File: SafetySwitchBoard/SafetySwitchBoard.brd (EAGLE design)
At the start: 47 x 73.7 mm, 10 parts

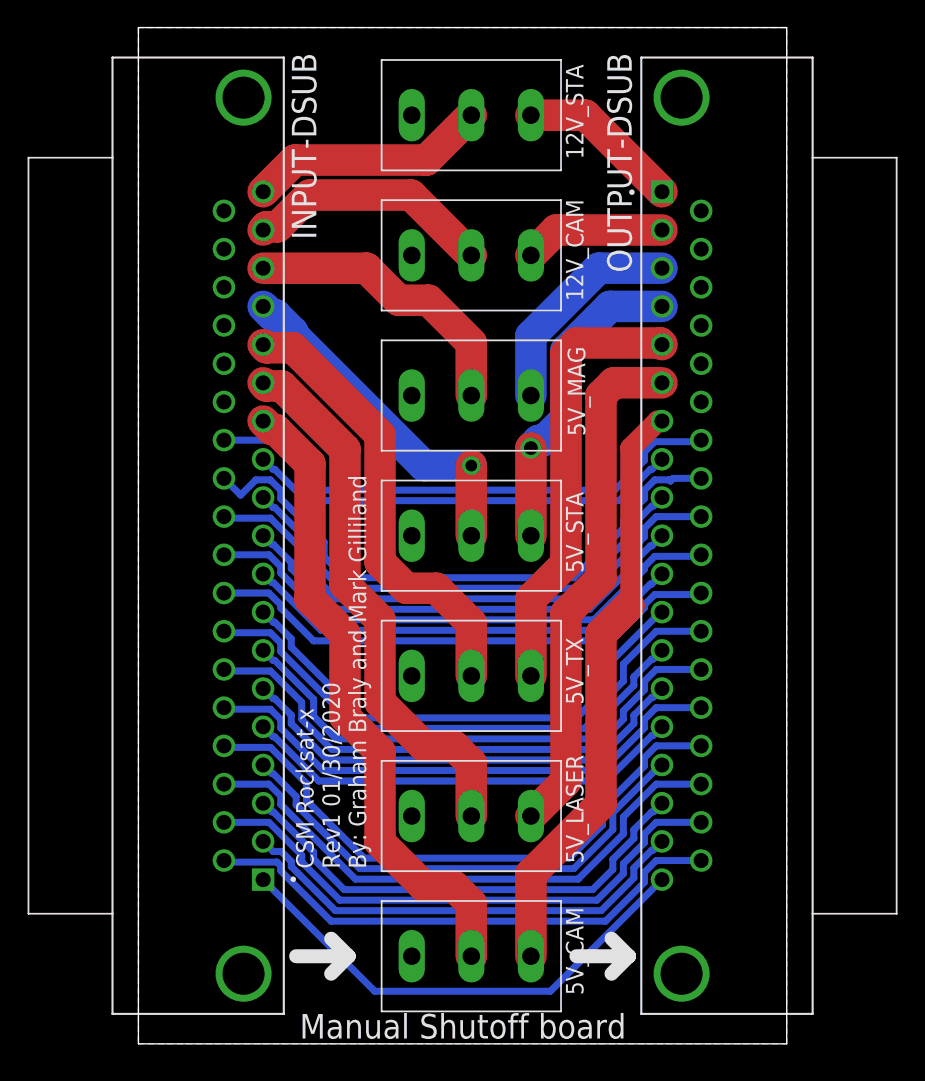
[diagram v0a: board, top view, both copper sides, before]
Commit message: Switch board diff pair rerouted
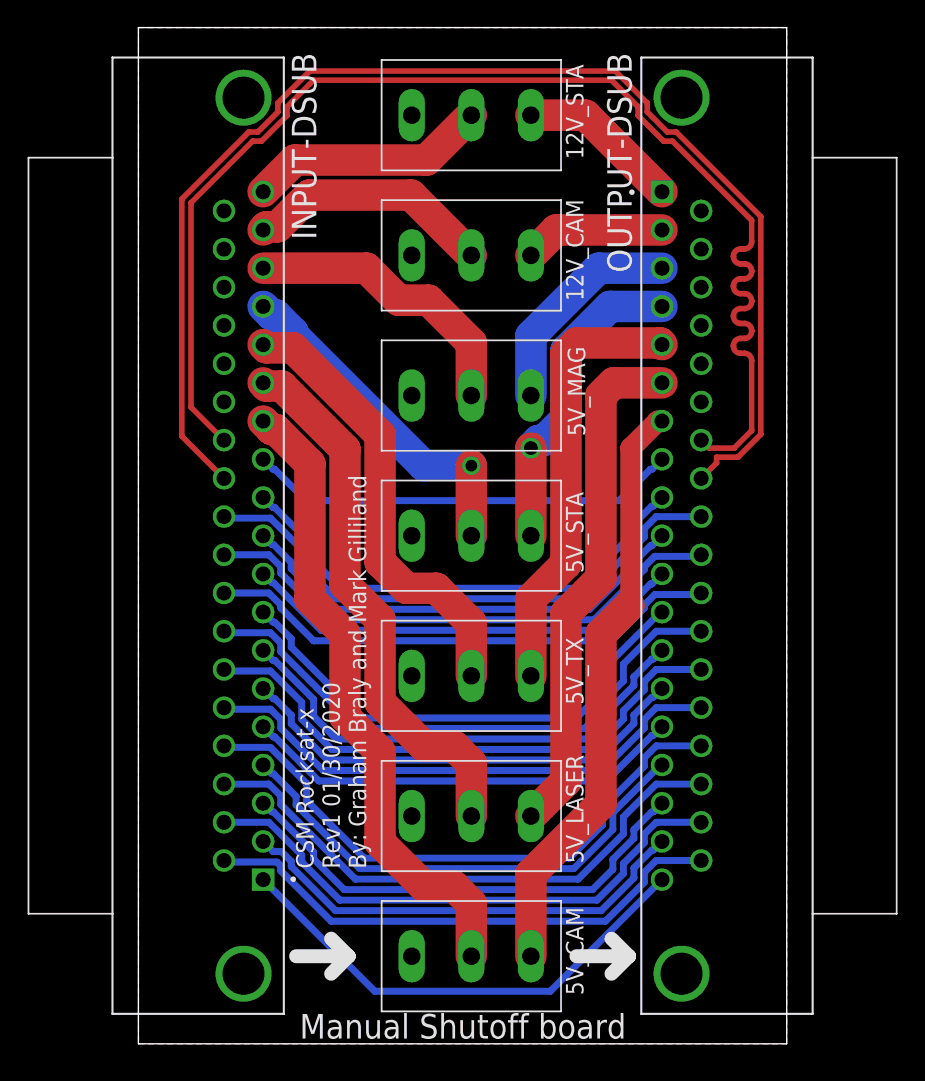
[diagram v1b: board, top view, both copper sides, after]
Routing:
- net USB-CAM_N: track 38.0 -> 92.8 mm
- net USB-CAM_P: track 43.2 -> 94.1 mm
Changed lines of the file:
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@@
 <class number="0" name="default" width="0" drill="0">
 </class>
-<class number="1" name="USB-DIFF" width="0" drill="0">
+<class number="1" name="USB-DIFF" width="0.4064" drill="0">
+<clearance class="1" value="0.254"/>
 </class>
 </classes>
@@
 <contactref element="INPUT-DSUB" pad="26"/>
 <contactref element="OUTPUT-DSUB" pad="31"/>
-<wire x1="6.2" y1="43.755" x2="9.585" y2="43.755" width="0.508" layer="16"/>
-<wire x1="34.5240375" y1="40.132" x2="36.6753" y2="42.2832625" width="0.508" layer="16"/>
-<wire x1="36.6753" y1="42.2832625" x2="36.6753" y2="42.898" width="0.508" layer="16"/>
-<wire x1="36.6753" y1="42.898" x2="37.422" y2="43.6447" width="0.508" layer="16"/>
-<wire x1="40.6797" y1="43.6447" x2="40.79" y2="43.755" width="0.508" layer="16"/>
-<wire x1="9.585" y1="43.755" x2="13.208" y2="40.132" width="0.508" layer="16"/>
-<wire x1="13.208" y1="40.132" x2="34.5240375" y2="40.132" width="0.508" layer="16"/>
-<wire x1="37.422" y1="43.6447" x2="40.6797" y2="43.6447" width="0.508" layer="16"/>
+<wire x1="6.2" y1="43.755" x2="3.81" y2="46.145" width="0.4064" layer="1"/>
+<wire x1="3.81" y1="46.145" x2="3.81" y2="60.96" width="0.4064" layer="1"/>
+<wire x1="3.81" y1="60.96" x2="8.2794" y2="65.4294" width="0.4064" layer="1"/>
+<wire x1="8.2794" y1="65.4294" x2="8.925025" y2="65.4294" width="0.4064" layer="1"/>
+<wire x1="8.925025" y1="65.4294" x2="10.7706" y2="67.274975" width="0.4064" layer="1"/>
+<wire x1="10.7706" y1="67.274975" x2="10.7706" y2="67.9206" width="0.4064" layer="1"/>
+<wire x1="10.7706" y1="67.9206" x2="12.7" y2="69.85" width="0.4064" layer="1"/>
+<wire x1="34.29" y1="69.85" x2="36.2194" y2="67.9206" width="0.4064" layer="1"/>
+<wire x1="36.2194" y1="67.9206" x2="36.2194" y2="67.274975" width="0.4064" layer="1"/>
+<wire x1="36.2194" y1="67.274975" x2="38.064975" y2="65.4294" width="0.4064" layer="1"/>
+<wire x1="38.064975" y1="65.4294" x2="38.7106" y2="65.4294" width="0.4064" layer="1"/>
+<wire x1="44.45" y1="44.45" x2="43.18" y2="43.18" width="0.4064" layer="1"/>
+<wire x1="12.7" y1="69.85" x2="34.29" y2="69.85" width="0.4064" layer="1"/>
+<wire x1="38.7106" y1="65.4294" x2="44.45" y2="59.69" width="0.4064" layer="1"/>
+<wire x1="44.45" y1="59.69" x2="44.45" y2="58.1392375" width="0.4064" layer="1"/>
+<wire x1="44.45" y1="58.1392375" x2="43.9293" y2="57.6185375" width="0.4064" layer="1" curve="-90"/>
+<wire x1="43.9293" y1="57.6185375" x2="43.652925" y2="57.6185375" width="0.4064" layer="1"/>
+<wire x1="43.652925" y1="57.6185375" x2="43.132225" y2="57.0978375" width="0.4064" layer="1" curve="90"/>
+<wire x1="43.132225" y1="57.0978375" x2="43.132225" y2="57.05811875" width="0.4064" layer="1"/>
+<wire x1="43.132225" y1="57.05811875" x2="43.652925" y2="56.53741875" width="0.4064" layer="1" curve="90"/>
+<wire x1="43.652925" y1="56.53741875" x2="43.9293" y2="56.53741875" width="0.4064" layer="1"/>
+<wire x1="43.9293" y1="56.53741875" x2="44.45" y2="56.01671875" width="0.4064" layer="1" curve="-90"/>
+<wire x1="44.45" y1="56.01671875" x2="44.45" y2="55.976996875" width="0.4064" layer="1"/>
+<wire x1="44.45" y1="55.976996875" x2="43.9293" y2="55.456296875" width="0.4064" layer="1" curve="-90"/>
+<wire x1="43.9293" y1="55.456296875" x2="43.652925" y2="55.456296875" width="0.4064" layer="1"/>
+<wire x1="43.652925" y1="55.456296875" x2="43.132225" y2="54.935596875" width="0.4064" layer="1" curve="90"/>
+<wire x1="43.132225" y1="54.935596875" x2="43.132225" y2="54.895878125" width="0.4064" layer="1"/>
+<wire x1="43.132225" y1="54.895878125" x2="43.652925" y2="54.375178125" width="0.4064" layer="1" curve="90"/>
+<wire x1="43.652925" y1="54.375178125" x2="43.9293" y2="54.375178125" width="0.4064" layer="1"/>
+<wire x1="43.9293" y1="54.375178125" x2="44.45" y2="53.854478125" width="0.4064" layer="1" curve="-90"/>
+<wire x1="44.45" y1="53.854478125" x2="44.45" y2="53.814759375" width="0.4064" layer="1"/>
+<wire x1="44.45" y1="53.814759375" x2="43.9293" y2="53.294059375" width="0.4064" layer="1" curve="-90"/>
+<wire x1="43.9293" y1="53.294059375" x2="43.652925" y2="53.294059375" width="0.4064" layer="1"/>
+<wire x1="43.652925" y1="53.294059375" x2="43.132225" y2="52.773359375" width="0.4064" layer="1" curve="90"/>
+<wire x1="43.132225" y1="52.773359375" x2="43.132225" y2="52.733640625" width="0.4064" layer="1"/>
+<wire x1="43.132225" y1="52.733640625" x2="43.652925" y2="52.212940625" width="0.4064" layer="1" curve="90"/>
+<wire x1="43.652925" y1="52.212940625" x2="43.9293" y2="52.212940625" width="0.4064" layer="1"/>
+<wire x1="43.9293" y1="52.212940625" x2="44.45" y2="51.692240625" width="0.4064" layer="1" curve="-90"/>
+<wire x1="44.45" y1="51.692240625" x2="44.45" y2="51.65251875" width="0.4064" layer="1"/>
+<wire x1="44.45" y1="51.65251875" x2="43.9293" y2="51.13181875" width="0.4064" layer="1" curve="-90"/>
+<wire x1="43.9293" y1="51.13181875" x2="43.652925" y2="51.13181875" width="0.4064" layer="1"/>
+<wire x1="43.652925" y1="51.13181875" x2="43.132225" y2="50.61111875" width="0.4064" layer="1" curve="90"/>
+<wire x1="43.132225" y1="50.61111875" x2="43.132225" y2="50.5714" width="0.4064" layer="1"/>
+<wire x1="43.132225" y1="50.5714" x2="43.652925" y2="50.0507" width="0.4064" layer="1" curve="90"/>
+<wire x1="43.652925" y1="50.0507" x2="43.9293" y2="50.0507" width="0.4064" layer="1"/>
+<wire x1="43.9293" y1="50.0507" x2="44.45" y2="49.53" width="0.4064" layer="1" curve="-90"/>
+<wire x1="44.45" y1="49.53" x2="44.45" y2="44.45" width="0.4064" layer="1"/>
+<wire x1="41.365" y1="43.18" x2="40.79" y2="43.755" width="0.4064" layer="1"/>
+<wire x1="43.18" y1="43.18" x2="41.365" y2="43.18" width="0.4064" layer="1"/>
 </signal>
 <signal name="USB-CAM_P" class="1">
 <contactref element="INPUT-DSUB" pad="27"/>
 <contactref element="OUTPUT-DSUB" pad="30"/>
-<wire x1="8.512" y1="40.8747" x2="9.568" y2="40.8747" width="0.508" layer="16"/>
-<wire x1="9.568" y1="40.8747" x2="10.3147" y2="40.128" width="0.508" layer="16"/>
-<wire x1="10.3147" y1="40.128" x2="10.3147" y2="39.5132625" width="0.508" layer="16"/>
-<wire x1="10.3147" y1="39.5132625" x2="13.462" y2="36.3659625" width="0.508" layer="16"/>
-<wire x1="13.462" y1="35.298525" x2="14.978525" y2="33.782" width="0.508" layer="16"/>
-<wire x1="13.462" y1="36.3659625" x2="13.462" y2="35.298525" width="0.508" layer="16"/>
-<wire x1="6.2" y1="40.985" x2="7.41115" y2="39.77385" width="0.508" layer="16"/>
-<wire x1="7.41115" y1="39.77385" x2="8.512" y2="40.8747" width="0.508" layer="16"/>
-<wire x1="38.761775" y1="40.985" x2="40.79" y2="40.985" width="0.508" layer="16"/>
-<wire x1="35.1513" y1="37.374525" x2="35.1513" y2="37.9892625" width="0.508" layer="16"/>
-<wire x1="36.6753" y1="39.5132625" x2="36.6753" y2="40.128" width="0.508" layer="16"/>
-<wire x1="36.6753" y1="40.128" x2="37.422" y2="40.8747" width="0.508" layer="16"/>
-<wire x1="37.422" y1="40.8747" x2="38.478" y2="40.8747" width="0.508" layer="16"/>
-<wire x1="38.478" y1="40.8747" x2="38.5647375" y2="40.7879625" width="0.508" layer="16"/>
-<wire x1="38.5647375" y1="40.7879625" x2="38.761775" y2="40.985" width="0.508" layer="16"/>
-<wire x1="35.1513" y1="37.9892625" x2="36.6753" y2="39.5132625" width="0.508" layer="16"/>
-<wire x1="14.978525" y1="33.782" x2="31.558775" y2="33.782" width="0.508" layer="16"/>
-<wire x1="31.558775" y1="33.782" x2="35.1513" y2="37.374525" width="0.508" layer="16"/>
+<wire x1="6.2" y1="40.985" x2="3.1496" y2="44.0354" width="0.4064" layer="1"/>
+<wire x1="3.1496" y1="61.23355" x2="8.00585" y2="66.0898" width="0.4064" layer="1"/>
+<wire x1="10.1102" y1="68.19415" x2="12.42645" y2="70.5104" width="0.4064" layer="1"/>
+<wire x1="8.00585" y1="66.0898" x2="8.651475" y2="66.0898" width="0.4064" layer="1"/>
+<wire x1="8.651475" y1="66.0898" x2="10.1102" y2="67.548525" width="0.4064" layer="1"/>
+<wire x1="10.1102" y1="67.548525" x2="10.1102" y2="68.19415" width="0.4064" layer="1"/>
+<wire x1="34.56355" y1="70.5104" x2="36.8798" y2="68.19415" width="0.4064" layer="1"/>
+<wire x1="36.8798" y1="68.19415" x2="36.8798" y2="67.548525" width="0.4064" layer="1"/>
+<wire x1="36.8798" y1="67.548525" x2="38.338525" y2="66.0898" width="0.4064" layer="1"/>
+<wire x1="38.338525" y1="66.0898" x2="38.98415" y2="66.0898" width="0.4064" layer="1"/>
+<wire x1="43.45355" y1="42.5196" x2="41.91" y2="42.5196" width="0.4064" layer="1"/>
+<wire x1="3.1496" y1="44.0354" x2="3.1496" y2="61.23355" width="0.4064" layer="1"/>
+<wire x1="12.42645" y1="70.5104" x2="34.56355" y2="70.5104" width="0.4064" layer="1"/>
+<wire x1="38.98415" y1="66.0898" x2="45.1104" y2="59.96355" width="0.4064" layer="1"/>
+<wire x1="45.1104" y1="59.96355" x2="45.1104" y2="44.17645" width="0.4064" layer="1"/>
+<wire x1="45.1104" y1="44.17645" x2="43.45355" y2="42.5196" width="0.4064" layer="1"/>
+<wire x1="41.91" y1="42.105" x2="40.79" y2="40.985" width="0.4064" layer="1"/>
+<wire x1="41.91" y1="42.5196" x2="41.91" y2="42.105" width="0.4064" layer="1"/>
 </signal>
 <signal name="BOOM-I2C-SCL">
